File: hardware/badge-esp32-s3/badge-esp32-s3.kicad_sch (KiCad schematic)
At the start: 4 parts, among them U1 ESP32-S3-WROOM-1(N16R8)

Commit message: Add empty sub schematics
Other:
- added sheet Audio (audio.kicad_sch)
- added sheet Charging (Charging.kicad_sch)
- added sheet Exposed Pins (exposed_pins.kicad_sch)
- added sheet LEDs (leds.kicad_sch)
- added sheet Onboard Peripheral (onboard_peripheral.kicad_sch)
- added sheet SD Card (sd_card.kicad_sch)

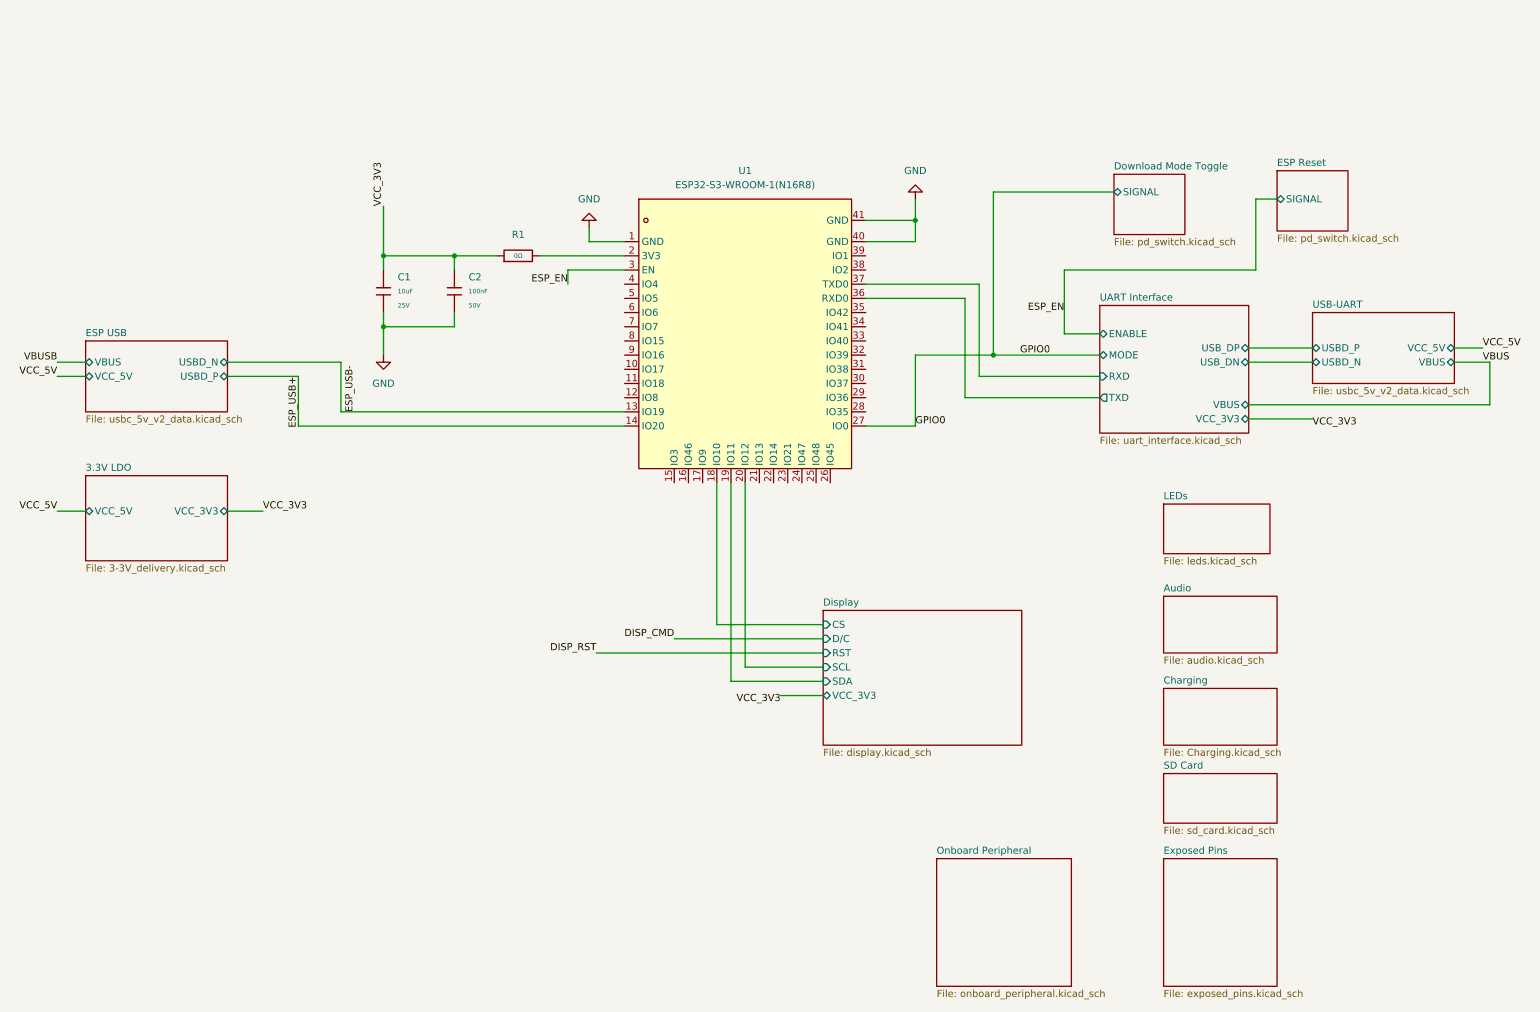
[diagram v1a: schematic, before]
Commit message: Incremental root schematic change
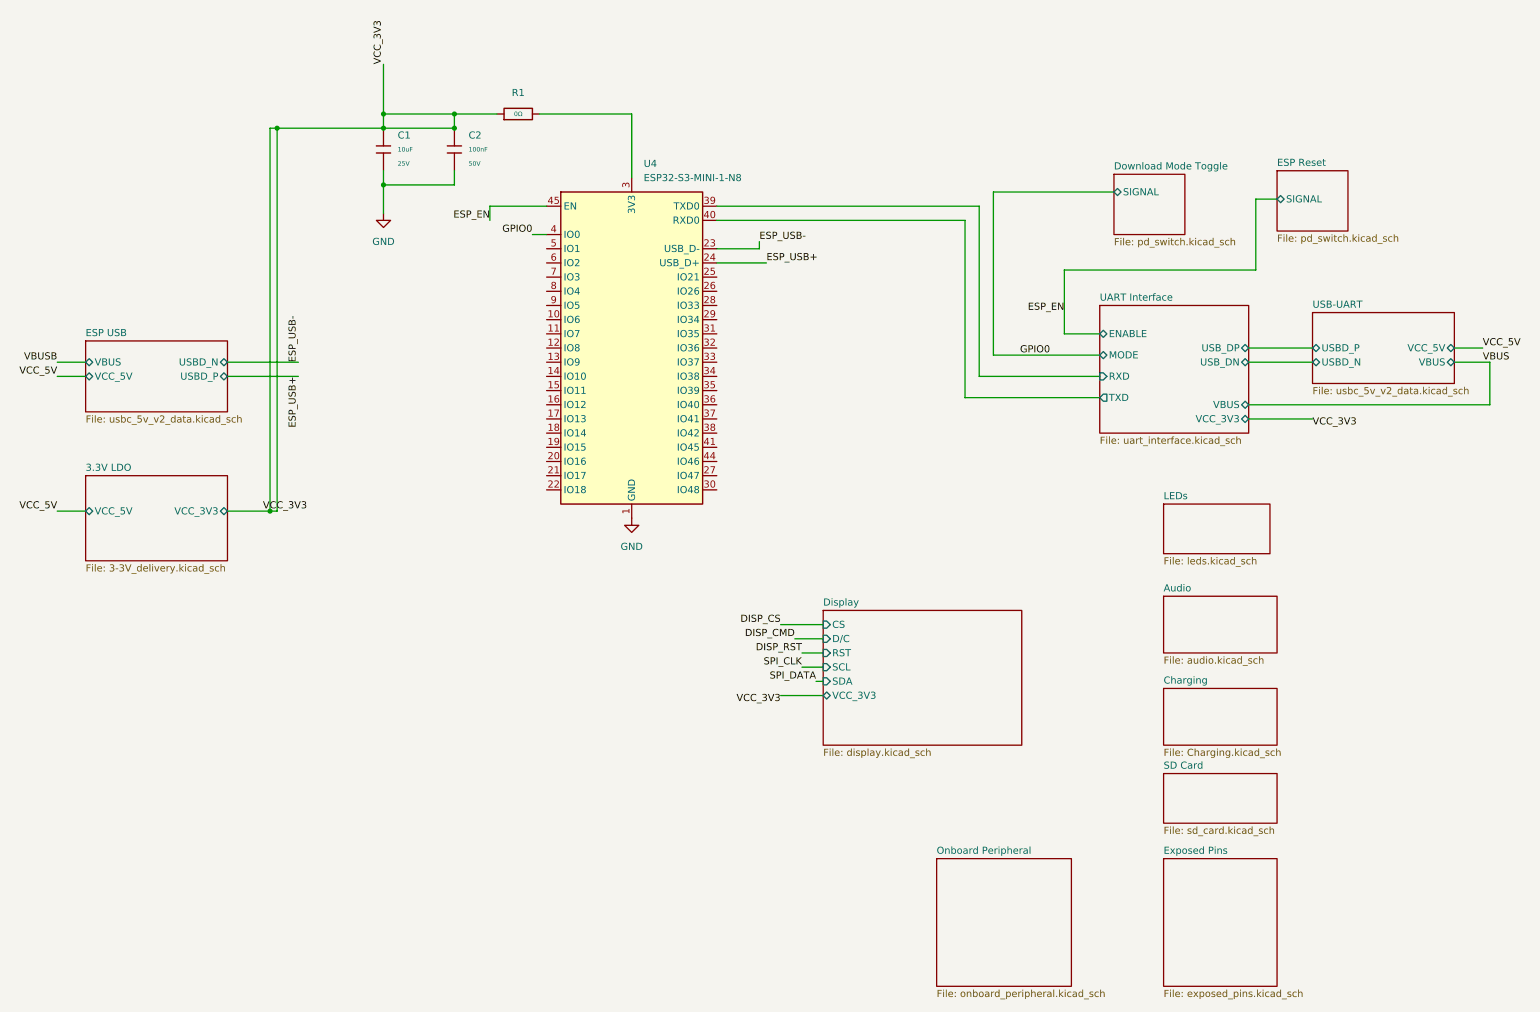
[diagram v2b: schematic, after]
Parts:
- removed U1: ESP32-S3-WROOM-1(N16R8), lcsc-lib:WIRELM-SMD_ESP32-S3-WROOM-1, symbol lcsc-lib:ESP32-S3-WROOM-1(N16R8)
- added U4: ESP32-S3-MINI-1-N8, RF_Module:ESP32-S2-MINI-1, symbol lcsc-lib:ESP32-S3-MINI-1-N8
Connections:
- net ESP_EN: now also U4.45 (EN)
- net ESP_USB+: now also U4.24 (USB_D+)
- net ESP_USB-: now also U4.23 (USB_D-)
- net GND: now also U4.1 (GND), U4.2 (GND), U4.42 (GND), U4.43 (GND), U4.46 (GND), U4.47 (GND), U4.48 (GND), U4.49 (GND), U4.50 (GND), U4.51 (GND), U4.52 (GND), U4.53 (GND), U4.54 (GND), U4.55 (GND), U4.56 (GND), U4.57 (GND), U4.58 (GND), U4.59 (GND), U4.60 (GND), U4.61 (GND), U4.62 (GND), U4.63 (GND), U4.64 (GND), U4.65 (GND)
- net GPIO0: now also U4.4 (IO0)
- net UART Interface/RXD: now also U4.39 (TXD0)
- net UART Interface/TXD: now also U4.40 (RXD0)
- net at R1.2: now also U4.3 (3V3)
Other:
- moved on the sheet: C1, C2, R1
